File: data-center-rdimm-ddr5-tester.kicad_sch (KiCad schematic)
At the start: 2 parts

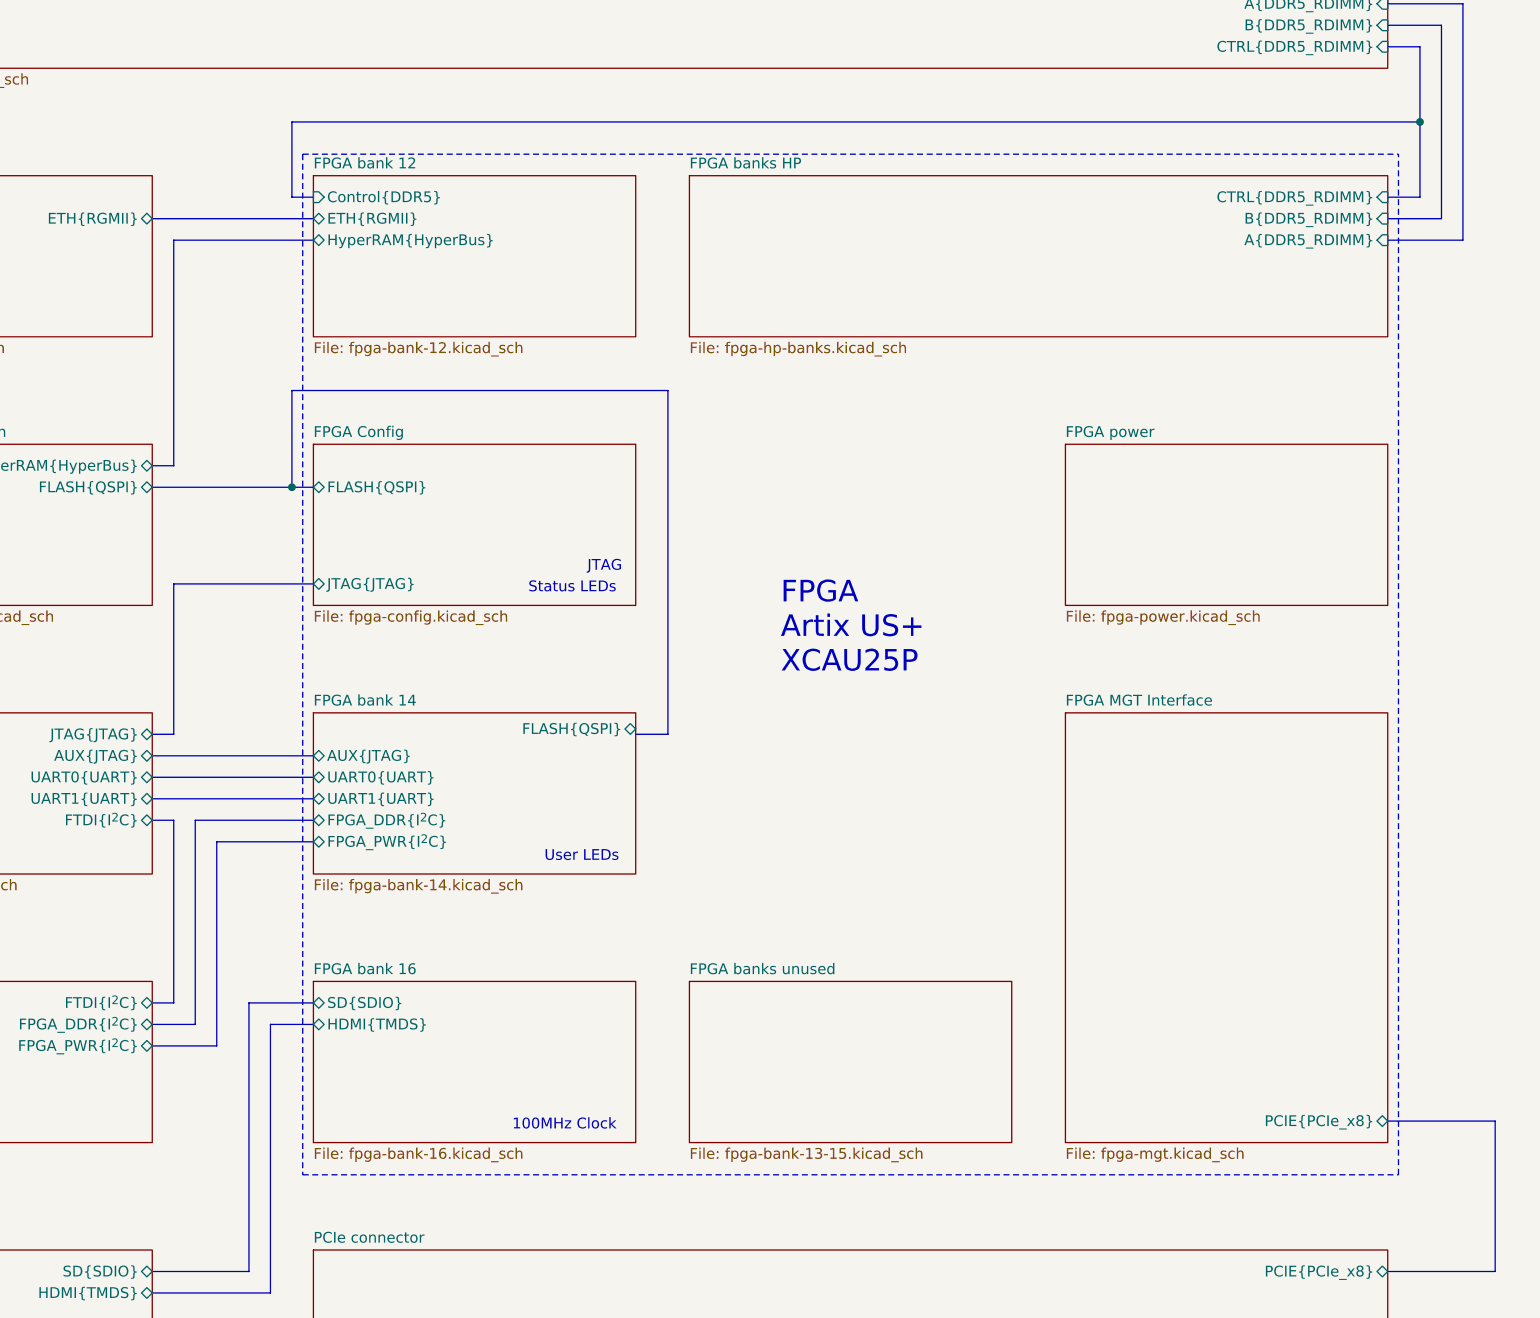
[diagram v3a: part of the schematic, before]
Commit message: [#66727] Finish connecting HDMI driver. Add SD card logic level converter. Add SD 3.0 support
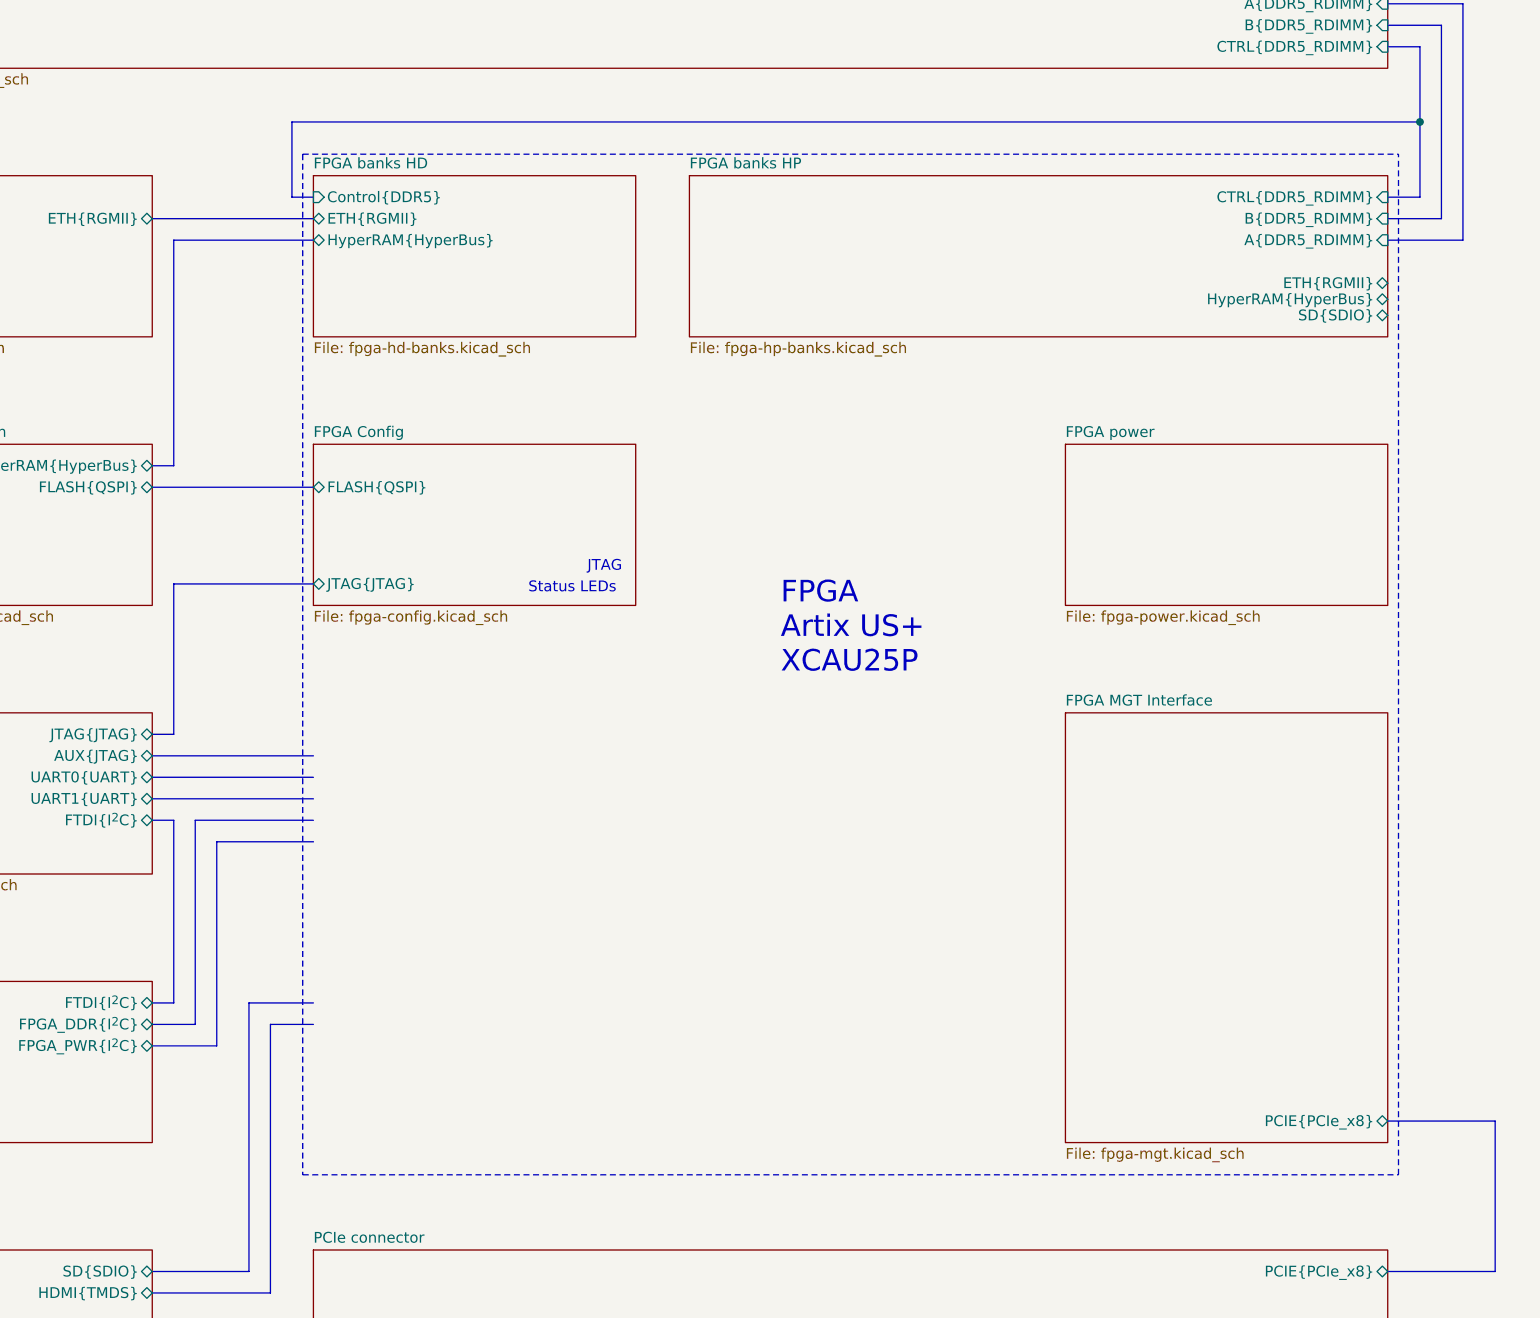
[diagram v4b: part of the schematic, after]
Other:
- sheet FPGA bank 12 renamed FPGA banks HD
- removed sheet FPGA bank 14
- removed sheet FPGA bank 16
- removed sheet FPGA banks unused
- sheet FPGA banks HD: file fpga-bank-12.kicad_sch -> fpga-hd-banks.kicad_sch
- sheet FPGA banks HP ports: added ETH{RGMII}, HyperRAM{HyperBus}, SD{SDIO}; removed none
- note removed: "100MHz Clock"
- note removed: "User LEDs"
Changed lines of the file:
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@@
   (junction (at 276.86 76.2) (diameter 0) (color 0 0 0 0)
   )
-  (junction (at 143.51 119.38) (diameter 0) (color 0 0 0 0)
-  )
   (bus (pts (xy 127 153.67) (xy 146.05 153.67))
     (stroke (width 0) (type default))
@@
   )
   (bus (pts (xy 129.54 180.34) (xy 129.54 158.75))
-    (stroke (width 0) (type default))
-  )
-  (bus (pts (xy 187.96 148.59) (xy 187.96 107.95))
     (stroke (width 0) (type default))
   )
@@
     (stroke (width 0) (type default))
   )
-  (bus (pts (xy 143.51 107.95) (xy 143.51 119.38))
-    (stroke (width 0) (type default))
-  )
   (polyline (pts (xy 144.78 80.01) (xy 274.32 80.01))
     (stroke (width 0) (type dash))
@@
     (stroke (width 0) (type default))
   )
-  (bus (pts (xy 143.51 119.38) (xy 146.05 119.38))
+  (bus (pts (xy 127 119.38) (xy 146.05 119.38))
     (stroke (width 0) (type default))
   )
@@
     (stroke (width 0) (type default))
   )
-  (bus (pts (xy 127 119.38) (xy 143.51 119.38))
-    (stroke (width 0) (type default))
-  )
-  (bus (pts (xy 187.96 107.95) (xy 143.51 107.95))
-    (stroke (width 0) (type default))
-  )
   (bus (pts (xy 127 182.88) (xy 132.08 182.88))
     (stroke (width 0) (type default))
@@
   )
   (bus (pts (xy 127 151.13) (xy 146.05 151.13))
-    (stroke (width 0) (type default))
-  )
-  (bus (pts (xy 184.15 148.59) (xy 187.96 148.59))
     (stroke (width 0) (type default))
   )
@@
     (effects (font (size 1.27 1.27)) (justify left bottom))
   )
-  (text "User LEDs" (at 173.355 163.83 0)
-    (effects (font (size 1.27 1.27)) (justify left bottom))
-  )
   (text "Mechanical" (at 254 259.715 0)
     (effects (font (size 1.27 1.27) (thickness 0.254) bold) (justify left bottom))
@@
   (text "RDIMM DDR5 Tester Ultrascale Plus" (at 172.085 35.56 0)
     (effects (font (size 3.9878 3.9878) (thickness 0.7976) bold) (justify left bottom))
-  )
-  (text "100MHz Clock" (at 169.545 195.58 0)
-    (effects (font (size 1.27 1.27)) (justify left bottom))
   )
   (symbol (lib_id "antmicroMechanicalParts:Heatsink_960-27-12-D-AB-0") (at 254 262.255 0) (unit 1)
@@
       (effects (font (size 1.27 1.27)) (justify right))
     )
+    (pin "ETH{RGMII}" bidirectional (at 273.05 95.25 0)
+      (effects (font (size 1.27 1.27)) (justify right))
+    )
+    (pin "HyperRAM{HyperBus}" bidirectional (at 273.05 97.155 0)
+      (effects (font (size 1.27 1.27)) (justify right))
+    )
+    (pin "SD{SDIO}" bidirectional (at 273.05 99.06 0)
+      (effects (font (size 1.27 1.27)) (justify right))
+    )
     (instances
       (project "data-center-rdimm-ddr5-tester"
@@
     )
   )
-  (sheet (at 146.05 146.05) (size 38.1 19.05) (fields_autoplaced)
-    (stroke (width 0.1524) (type solid))
-    (fill (color 0 0 0 0.0000))
-    (property "Sheetname" "FPGA bank 14" (at 146.05 145.3384 0)
-      (effects (font (size 1.27 1.27)) (justify left bottom))
-    )
-    (property "Sheetfile" "fpga-bank-14.kicad_sch" (at 146.05 165.6846 0)
-      (effects (font (size 1.27 1.27)) (justify left top))
-    )
-    (pin "FLASH{QSPI}" bidirectional (at 184.15 147.955 0)
-      (effects (font (size 1.27 1.27)) (justify right))
-    )
-    (pin "UART0{UART}" bidirectional (at 146.05 153.67 180)
-      (effects (font (size 1.27 1.27)) (justify left))
-    )
-    (pin "AUX{JTAG}" bidirectional (at 146.05 151.13 180)
-      (effects (font (size 1.27 1.27)) (justify left))
-    )
-    (pin "UART1{UART}" bidirectional (at 146.05 156.21 180)
-      (effects (font (size 1.27 1.27)) (justify left))
-    )
-    (pin "FPGA_PWR{I^{2}C}" bidirectional (at 146.05 161.29 180)
-      (effects (font (size 1.27 1.27)) (justify left))
-    )
-    (pin "FPGA_DDR{I^{2}C}" bidirectional (at 146.05 158.75 180)
-      (effects (font (size 1.27 1.27)) (justify left))
-    )
-    (instances
-      (project "data-center-rdimm-ddr5-tester"
-        (path "/1faa6543-e26a-4449-8bac-ee14b9f19e5f" (page "15"))
-      )
-    )
-  )
   (sheet (at 146.05 82.55) (size 38.1 19.05) (fields_autoplaced)
     (stroke (width 0.1524) (type solid))
     (fill (color 0 0 0 0.0000))
-    (property "Sheetname" "FPGA bank 12" (at 146.05 81.8384 0)
+    (property "Sheetname" "FPGA banks HD" (at 146.05 81.8384 0)
       (effects (font (size 1.27 1.27)) (justify left bottom))
     )
-    (property "Sheetfile" "fpga-bank-12.kicad_sch" (at 146.05 102.1846 0)
+    (property "Sheetfile" "fpga-hd-banks.kicad_sch" (at 146.05 102.1846 0)
       (effects (font (size 1.27 1.27)) (justify left top))
     )
@@
       )
     )
-  )
-  (sheet (at 146.05 177.8) (size 38.1 19.05) (fields_autoplaced)
-    (stroke (width 0.1524) (type solid))
-    (fill (color 0 0 0 0.0000))
-    (property "Sheetname" "FPGA bank 16" (at 146.05 177.0884 0)
-      (effects (font (size 1.27 1.27)) (justify left bottom))
-    )
-    (property "Sheetfile" "fpga-bank-16.kicad_sch" (at 146.05 197.4346 0)
-      (effects (font (size 1.27 1.27)) (justify left top))
-    )
-    (pin "HDMI{TMDS}" bidirectional (at 146.05 182.88 180)
-      (effects (font (size 1.27 1.27)) (justify left))
-    )
-    (pin "SD{SDIO}" bidirectional (at 146.05 180.34 180)
-      (effects (font (size 1.27 1.27)) (justify left))
-    )
-    (instances
-      (project "data-center-rdimm-ddr5-tester"
-        (path "/1faa6543-e26a-4449-8bac-ee14b9f19e5f" (page "16"))
-      )
-    )
-  )
-  (sheet (at 190.5 177.8) (size 38.1 19.05) (fields_autoplaced)
-    (stroke (width 0.1524) (type solid))
-    (fill (color 0 0 0 0.0000))
-    (property "Sheetname" "FPGA banks unused" (at 190.5 177.0884 0)
-      (effects (font (size 1.27 1.27)) (justify left bottom))
-    )
-    (property "Sheetfile" "fpga-bank-13-15.kicad_sch" (at 190.5 197.4346 0)
-      (effects (font (size 1.27 1.27)) (justify left top))
-    )
-    (instances
-      (project "data-center-rdimm-ddr5-tester"
-        (path "/1faa6543-e26a-4449-8bac-ee14b9f19e5f" (page "14"))
-      )
-    )
